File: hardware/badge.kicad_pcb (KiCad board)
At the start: 2 copper layers, 88 x 156.6 mm, 122 parts, among them J1 Micro_SD_Card, J2 MY-18650-01, J3 Conn_01x40, J4 USB_C_Receptacle_USB2.0_14P, J5 MY-18650-01, Q1 AO3400A, Q3 AO3400A, SW1 SW_Push, SW10 SW_Push, SW11 SW_Push, SW12 SW_Push, SW13 SW_Push, SW14 SW_Push, SW15 SW_Push, SW16 SW_Push, SW17 SW_Push, SW18 SW_Push, SW19 SW_Push, SW2 SW_Push, SW20 SW_Push, SW21 SW_Push, SW22 SW_Push, SW23 SW_Push, SW25 SW_Push, SW26 SW_Push, SW27 SW_Push, SW28 SW_Push, SW29 SW_Push, SW3 SW_Push, SW30 SW_Push, SW31 SW_Push, SW33 SW_Push, SW34 SW_Push, SW35 SW_Push, SW36 SW_Push, SW37 SW_Push, SW38 SW_Push, SW39 SW_Push, SW4 SW_Push, SW5 SW_Push, SW57 MK-12C02-G020, SW58 SKRHABE010, SW6 SW_Push, SW7 SW_Push, SW8 BOOT, SW9 SW_Push, U1 ESP32-S3-WROOM-1, U10 PCA9555PW, U11 PCA9555PW, U3 BQ24075RGT, U4 TLV62569DBV, U5 BME280, U6 USBLC6-2P6, U7 BMI270, U8 Ai-Thinker-Ra-02, U9 MAX98357A

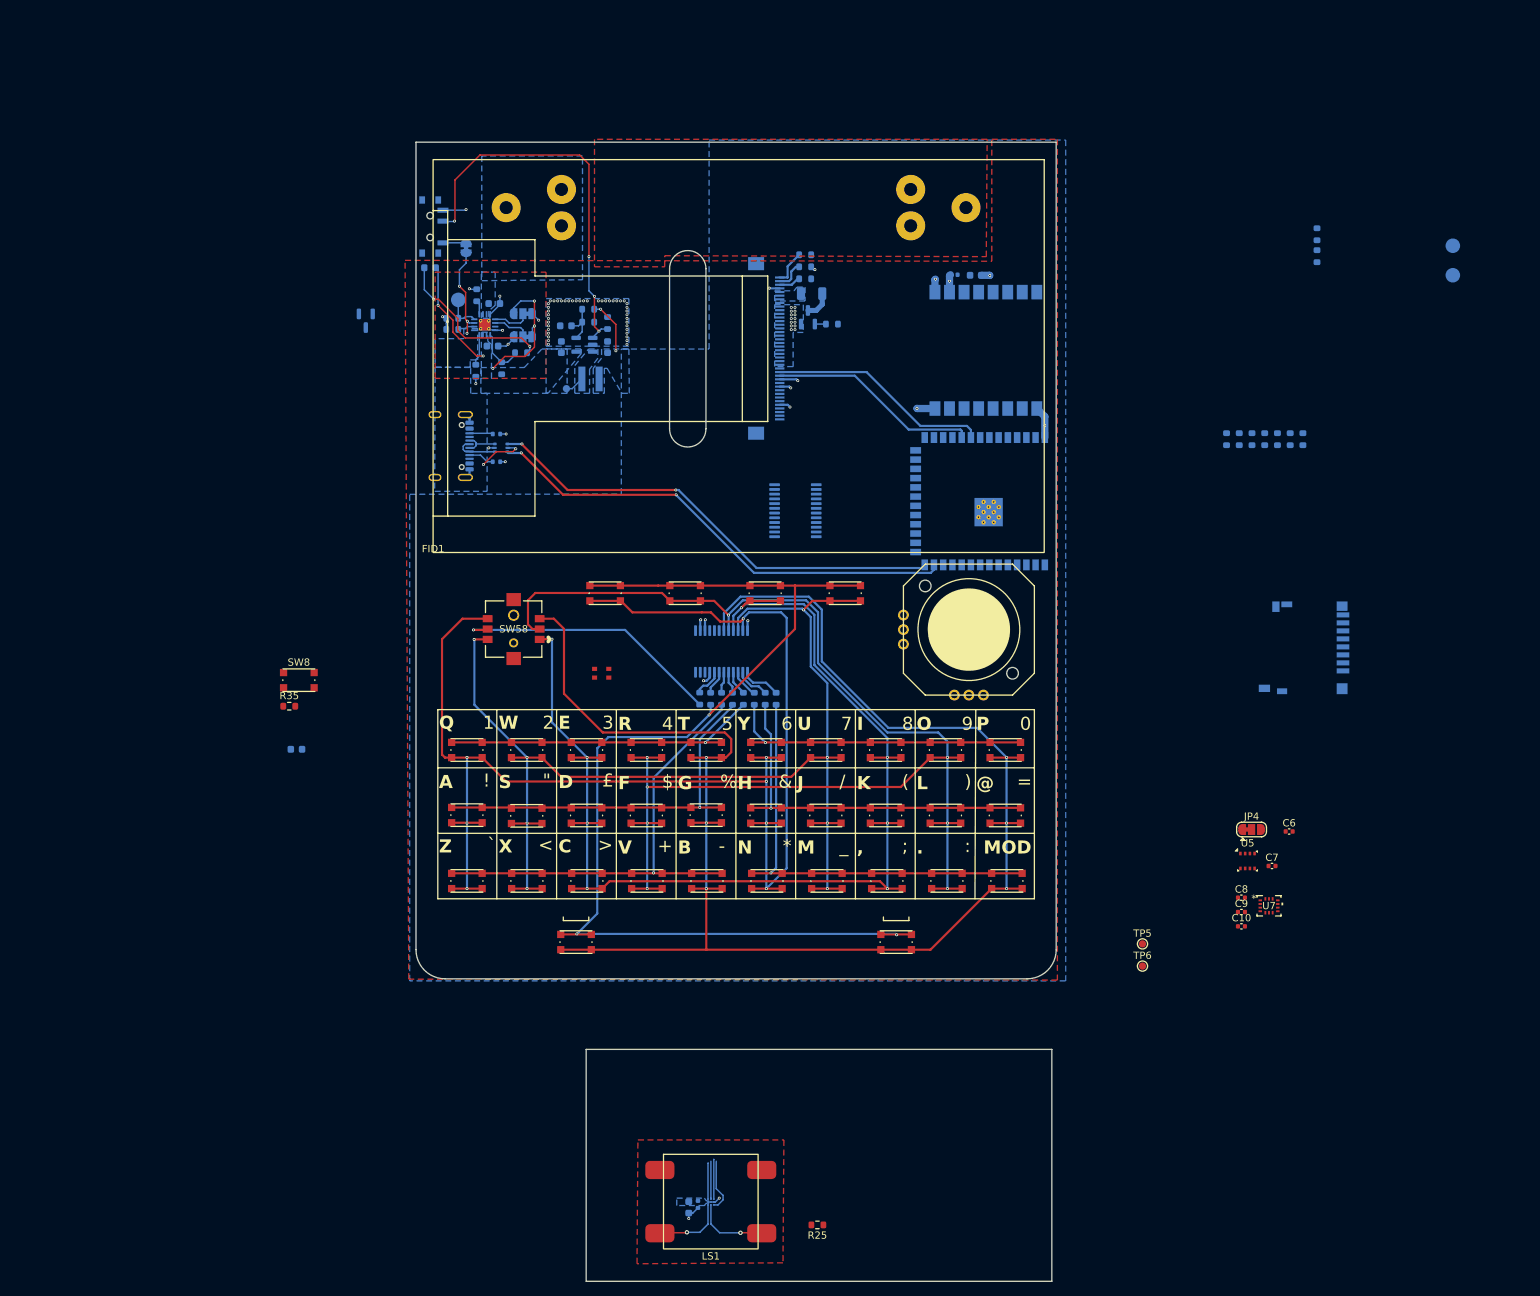
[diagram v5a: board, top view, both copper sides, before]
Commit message: Move usb to the opposite side of the PCB
Change the lcd SPI pins and use ones dirrectly atatched to SPI2
Lengh tune the LCD spi line and USB
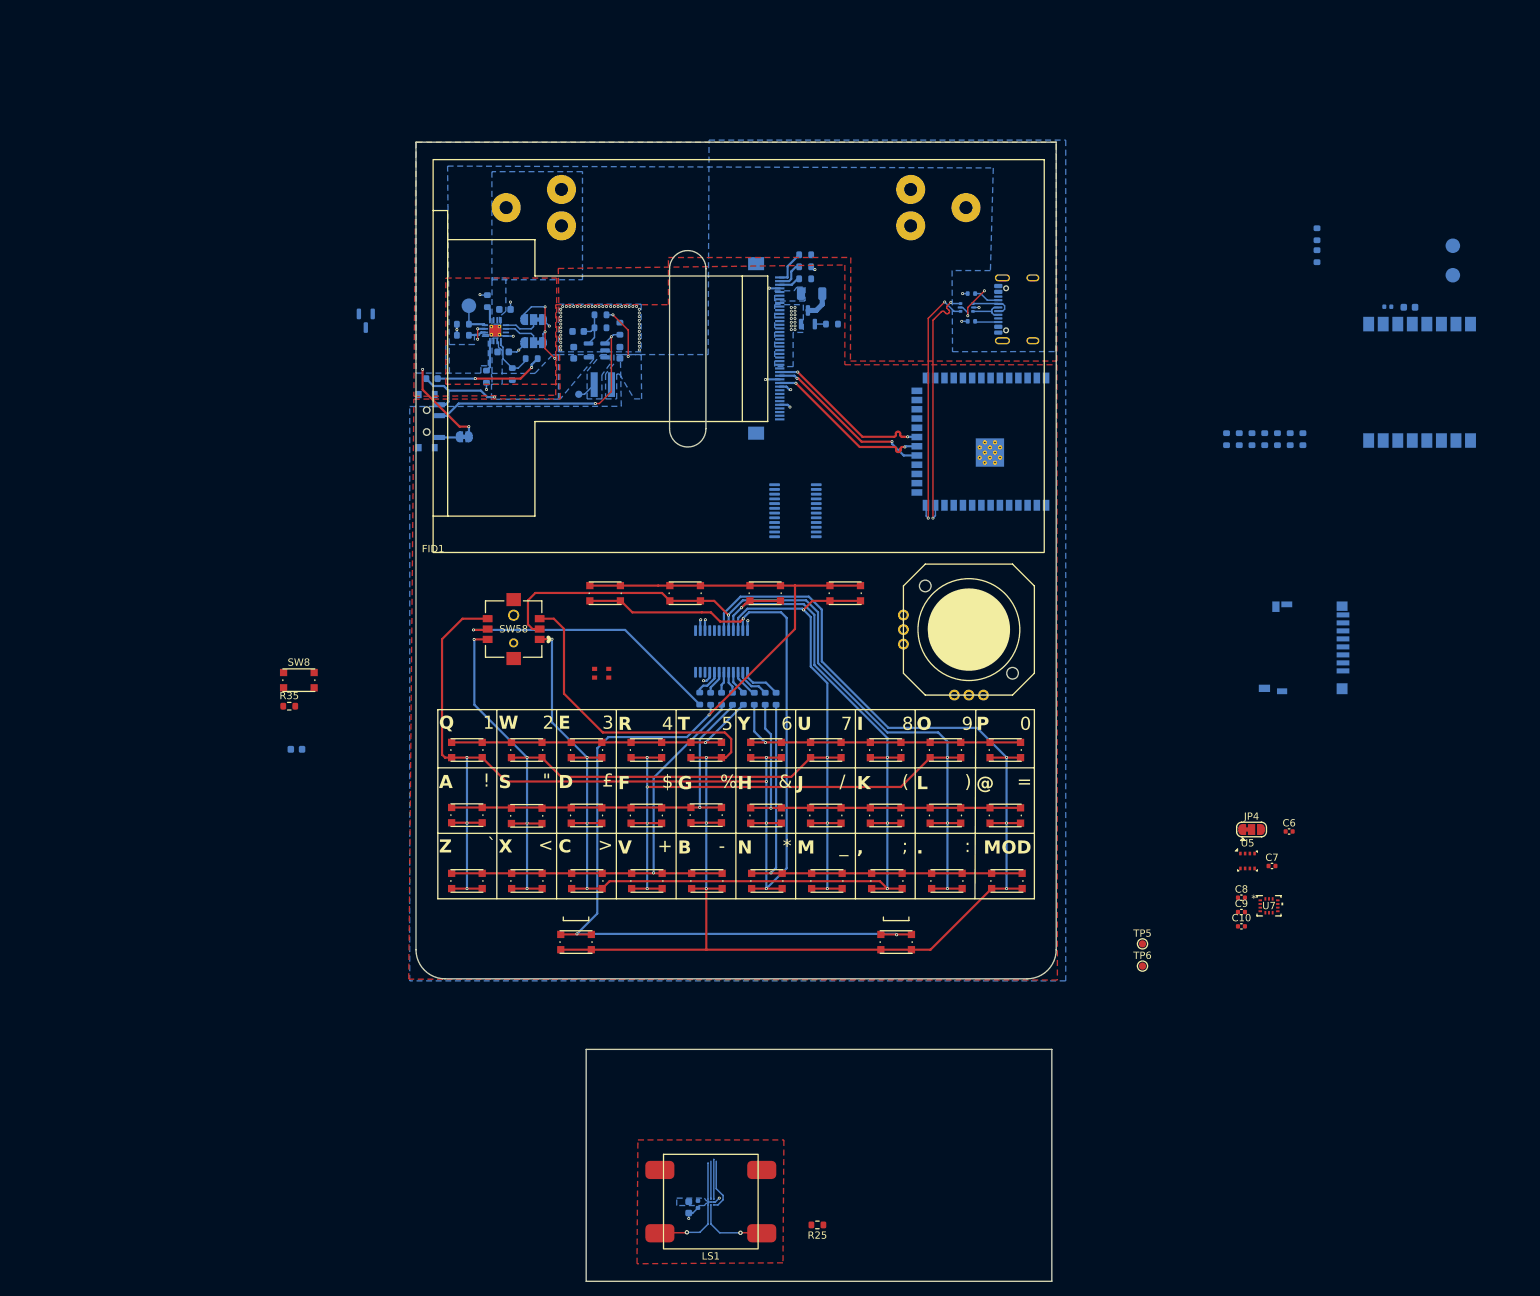
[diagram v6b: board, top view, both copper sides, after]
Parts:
- moved J4 82.2 mm to (164.7, 54.0), turned to -90 degrees
- moved R26 69.3 mm to (157.3, 51.8), turned to 180 degrees
- moved R27 67.1 mm to (157.3, 55.6), turned to 180 degrees
- moved U6 66.9 mm to (156.7, 53.7), turned to 180 degrees
- moved C11 59.8 mm to (214.6, 53.6)
- moved C12 59.8 mm to (217.6, 53.7)
- moved U8 59.8 mm to (218.9, 64.0)
- moved SW57 26.7 mm to (82.8, 69.3)
- moved JP3 25.9 mm to (87.6, 71.5), turned to 180 degrees
- moved D1 15.2 mm to (83.2, 63.5), turned to 180 degrees
- moved U1 8.19 mm to (162.3, 72.2)
- moved C1 1.86 mm to (102.7, 59.9)
- moved C2 1.86 mm to (103.3, 57.0)
- moved TP4 1.86 mm to (103.4, 65.7)
- moved L1 1.86 mm to (106.7, 64.3)
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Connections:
- U1 pad 18: unconnected-(U1-IO10-Pad18) -> /LCD.CS
- U1 pad 19: unconnected-(U1-IO11-Pad19) -> /LCD.MOSI
- U1 pad 20: /AUDIO.SD -> /LCD.CLK
- U1 pad 21: /AUDIO.LRCLK -> /LCD.MISO
- U1 pad 31: /LCD.MOSI -> unconnected-(U1-IO38-Pad31)
- U1 pad 32: /LCD.MISO -> unconnected-(U1-IO39-Pad32)
- U1 pad 33: /LCD.CLK -> unconnected-(U1-IO40-Pad33)
- U1 pad 8: unconnected-(U1-IO15-Pad8) -> /AUDIO.LRCLK
- U1 pad 9: unconnected-(U1-IO16-Pad9) -> /AUDIO.SD
- U10 pad 5: /LCD.CS -> unconnected-(U10-IO0_1-Pad5)
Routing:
- net /mcu/USB_D-: track 66.4 -> 35.2 mm
- net /mcu/USB_D+: track 64.7 -> 35.3 mm
- net /LCD.CLK: track 0.00 -> 23.5 mm, vias 0 -> 2
- net Net-(SW57-B): track 53.8 -> 35.1 mm, vias 4 -> 2
- net GND: track 50.2 -> 32.3 mm, vias 84 -> 80
- net VSYS: track 37.5 -> 26.7 mm, vias 6 -> 4
- net Net-(D1-K): track 22.8 -> 15.1 mm
- net /LCD.MISO: track 30.6 -> 23.5 mm, vias 0 -> 2
- net /LCD.MOSI: track 29.1 -> 23.6 mm, vias 0 -> 2
- net VUSB: track 19.4 -> 21.2 mm, vias 5 -> 6
- net Net-(JP3-B): track 3.29 -> 2.78 mm

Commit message: Route I2C bus
Add decoupling capacitors to esp32 and io expandes
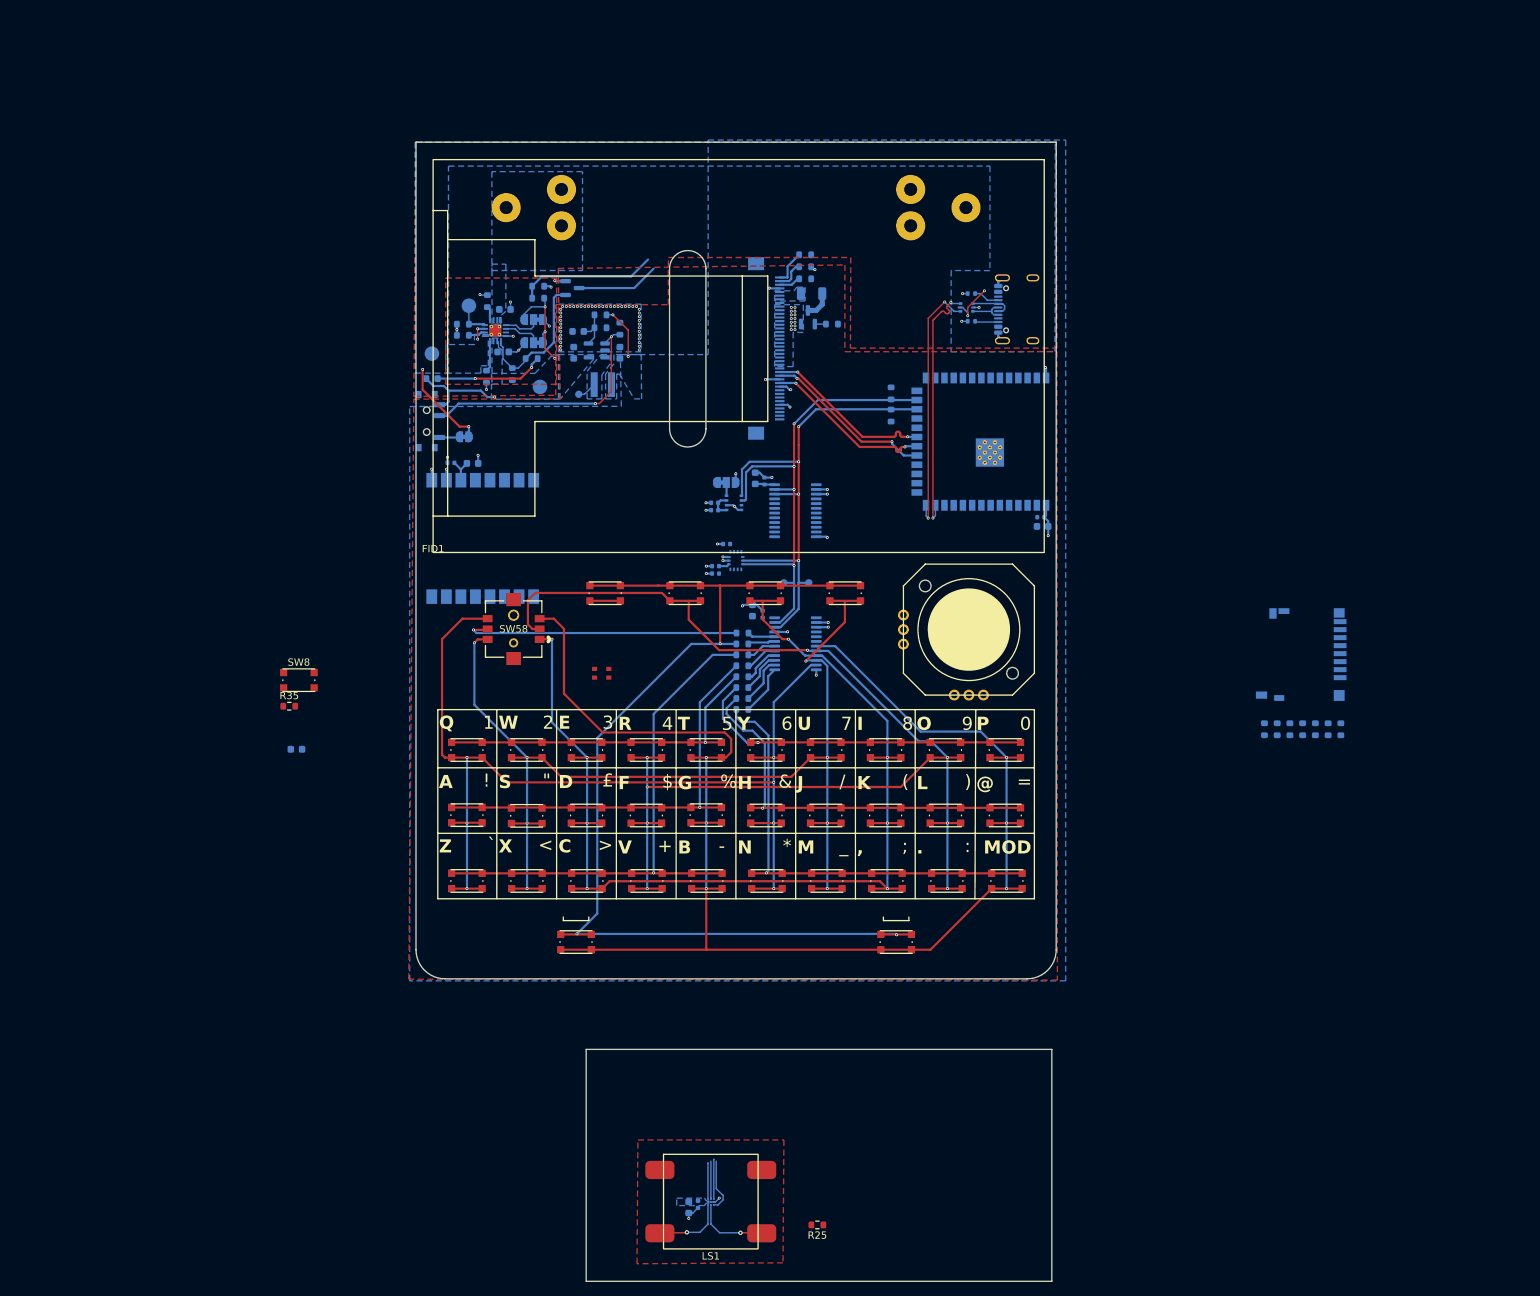
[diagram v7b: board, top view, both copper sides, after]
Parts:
- added C16: 10uF, Capacitor_SMD:C_0603_1608Metric, B.Cu at (127.6, 77.2)
- added C17: 100nF 6.3V, Capacitor_SMD:C_0402_1005Metric, B.Cu at (128.9, 77.6)
- added C18: 10uF, Capacitor_SMD:C_0603_1608Metric, B.Cu at (167.1, 83.8)
- added C19: 100nF 6.3V, Capacitor_SMD:C_0402_1005Metric, B.Cu at (166.9, 82.5)
- added C20: 10uF, Capacitor_SMD:C_0603_1608Metric, B.Cu at (127.3, 95.4)
- added C21: 100nF 6.3V, Capacitor_SMD:C_0402_1005Metric, B.Cu at (128.7, 95.9)
- added R36: 1.2k, Resistor_SMD:R_0603_1608Metric, B.Cu at (146.3, 65.5)
- added R37: 1.2k, Resistor_SMD:R_0603_1608Metric, B.Cu at (146.3, 68.6)
- C10, C6, C7, C8, C9, JP4, TP5, TP6, U5, U7: moved to B.Cu
- moved TP1 141.1 mm to (83.2, 60.1)
- moved U8 130.6 mm to (90.2, 85.5)
- moved C11 130.6 mm to (85.8, 75.1)
- moved C12 130.6 mm to (88.8, 75.2)
- moved TP2 126.4 mm to (98.0, 64.6)
- moved R33 107.3 mm to (97.8, 50.8), turned to 0 degrees
- moved R34 107.2 mm to (97.8, 52.5), turned to 180 degrees
- moved C6 91.0 mm to (122.0, 80.6), turned to 180 degrees
- moved C7 90.9 mm to (122.0, 81.6), turned to 180 degrees
- moved C10 88.1 mm to (123.7, 86.2), turned to 180 degrees
- moved U7 87.3 mm to (125.0, 88.5), turned to 90 degrees
- moved JP4 86.5 mm to (123.7, 77.8)
- moved C9 86.5 mm to (122.2, 89.3), turned to 180 degrees
- moved U5 86.1 mm to (124.7, 80.6), turned to 90 degrees
- moved C8 84.9 mm to (122.2, 90.3), turned to 180 degrees
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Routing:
- net /imu/SCL: track 0.00 -> 70.9 mm, vias 0 -> 4
- net /imu/SDA: track 0.00 -> 69.7 mm, vias 0 -> 4
- net Net-(U11-IO0_7): track 195.6 -> 147.3 mm, vias 8 -> 7
- net GND: track 32.3 -> 67.5 mm, vias 80 -> 102
- net Net-(U11-IO0_3): track 229.7 -> 206.7 mm
- net /mcu/VBAT_DIV2: track 0.00 -> 19.1 mm
- net /power/~{CHG}: track 6.91 -> 19.6 mm
- net +3.3V: track 7.47 -> 19.1 mm
- net /mcu/CHG: track 0.00 -> 11.3 mm
- net Net-(U11-IO0_6): track 162.8 -> 151.7 mm
- net Net-(R13-Pad2): track 64.2 -> 73.8 mm
- net Net-(U11-IO0_5): track 165.2 -> 156.1 mm
- net Net-(R14-Pad2): track 157.7 -> 150.1 mm
- net Net-(U11-IO0_4): track 183.7 -> 177.6 mm
- net Net-(R12-Pad2): track 53.0 -> 58.6 mm
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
